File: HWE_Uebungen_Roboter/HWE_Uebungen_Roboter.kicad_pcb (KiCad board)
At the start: 2 copper layers, 3 parts, among them IC1 TB67H450AFNG, U1 ATmega328-P

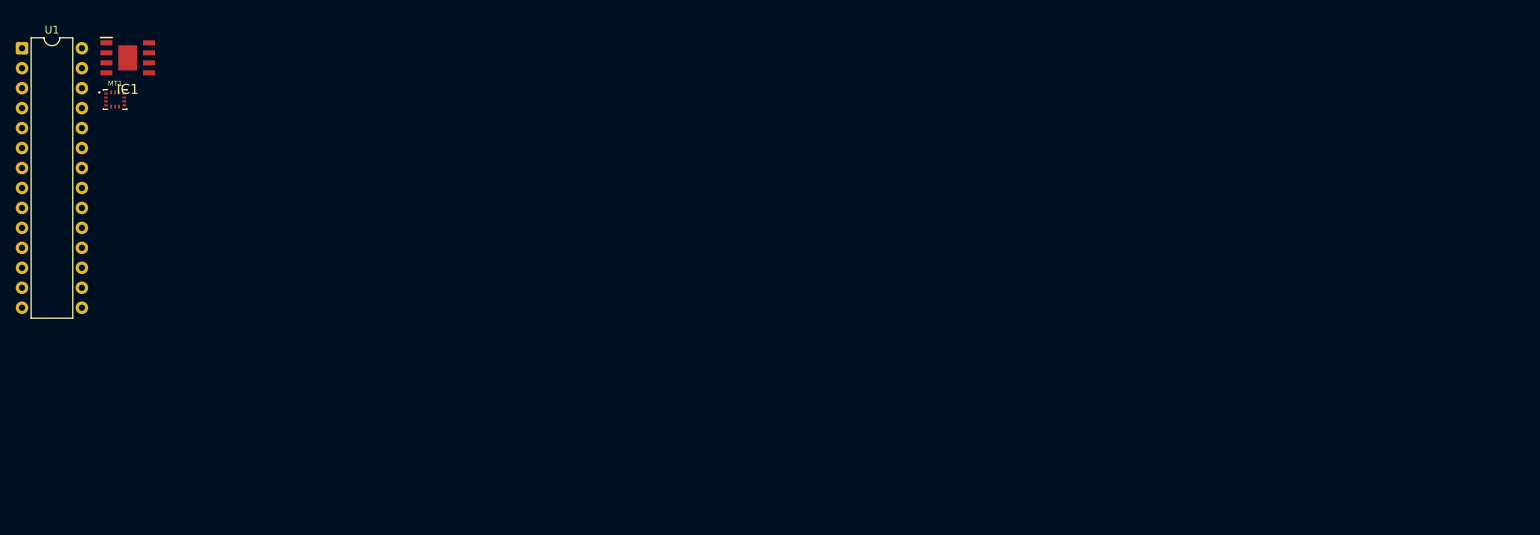
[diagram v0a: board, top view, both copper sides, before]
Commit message: Hardware-Zwischenstand mit KiCad-Projekt und Bestückungsunterlagen
Aktuellen Hardware-Entwicklungsstand des HWE-Roboters von Felix Mähr
und Linus Kimpfler mit bestehender Projektstruktur übernehmen.

Enthalten sind:
- KiCad-Projekt mit Schaltplan und PCB-Layout
- Eigene Symbol- und Footprint-Bibliotheken mit Bibliothekstabellen
- Datenblätter der vorgesehenen Bauteile
- Schaltplan- und PCB-Abbildungen sowie 3D-Vorschau
- Interaktive HTML-Stückliste als Bestückungshilfe

Stand vor der geplanten PCB-Bestellung; das Gesamtprojekt ist noch
nicht abgeschlossen. Softwareentwicklung, Inbetriebnahme und
Funktionsnachweise sind nicht Bestandteil dieses Zwischenstands.

Die ausführliche Projektdokumentation und die .gitignore werden
in einem separaten Commit ergänzt.
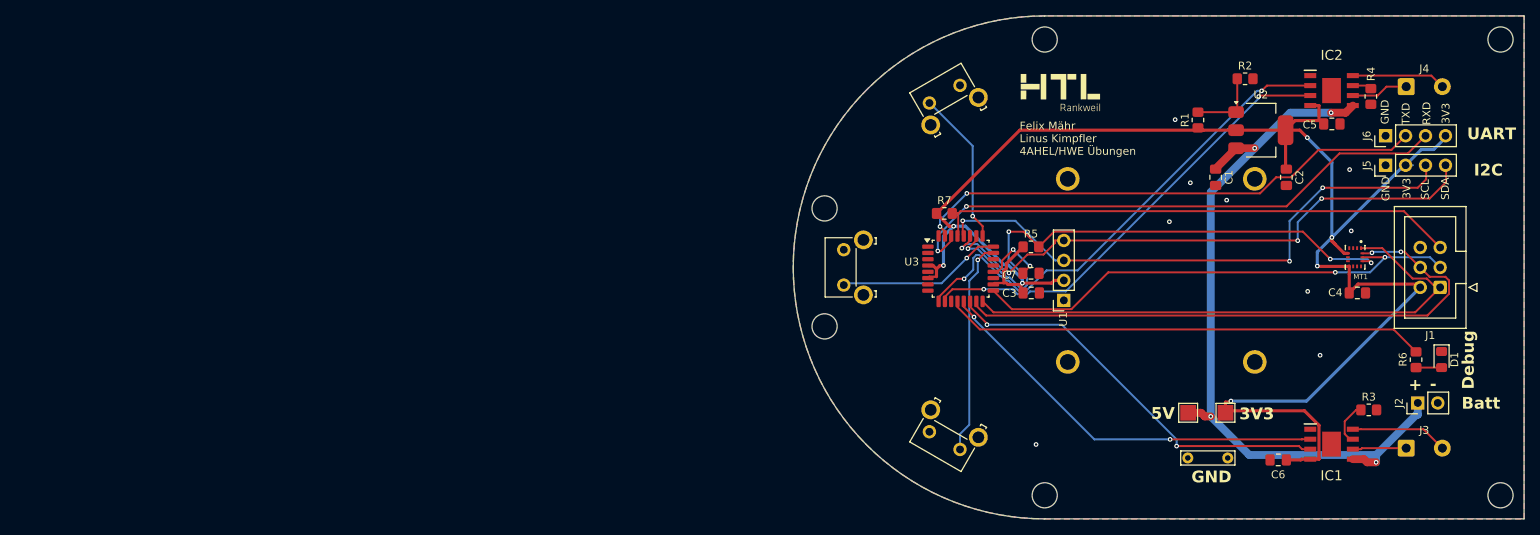
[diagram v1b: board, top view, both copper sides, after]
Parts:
- added C1: C, Capacitor_SMD:C_0805_2012Metric_Pad1.18x1.45mm_HandSolder, F.Cu at (190.5, 64.4)
- added C2: C, Capacitor_SMD:C_0805_2012Metric_Pad1.18x1.45mm_HandSolder, F.Cu at (199.5, 64.4)
- added C3: 100n, Capacitor_SMD:C_0805_2012Metric_Pad1.18x1.45mm_HandSolder, F.Cu at (167.1, 79.1)
- added C4: 100n, Capacitor_SMD:C_0805_2012Metric_Pad1.18x1.45mm_HandSolder, F.Cu at (208.6, 79.1)
- added C5: 100n, Capacitor_SMD:C_0805_2012Metric_Pad1.18x1.45mm_HandSolder, F.Cu at (205.3, 57.6)
- added C6: 100n, Capacitor_SMD:C_0805_2012Metric_Pad1.18x1.45mm_HandSolder, F.Cu at (198.5, 100.4)
- added C7: 100n, Capacitor_SMD:C_0805_2012Metric_Pad1.18x1.45mm_HandSolder, F.Cu at (167.0, 76.6)
- added D1: LED, LED_SMD:LED_0805_2012Metric_Pad1.15x1.40mm_HandSolder, F.Cu at (219.3, 87.6)
- added G***: LOGO, HWE_Lib:HTL_Logo, F.Cu at (170.8, 53.6)
- added H1: MountingHole, MountingHole:MountingHole_3.2mm_M3, F.Cu at (168.8, 46.9)
- added H2: MountingHole, MountingHole:MountingHole_3.2mm_M3, F.Cu at (168.8, 104.9)
- added H3: MountingHole, MountingHole:MountingHole_3.2mm_M3, F.Cu at (140.8, 68.4)
- added H4: MountingHole, MountingHole:MountingHole_3.2mm_M3, F.Cu at (140.8, 83.4)
- added H5: MountingHole, MountingHole:MountingHole_3.2mm_M3, F.Cu at (226.8, 46.9)
- added H6: MountingHole, MountingHole:MountingHole_3.2mm_M3, F.Cu at (226.8, 104.9)
- added IC2: TB67H450AFNG, Robo:P-HSOP8-0405-1.27-002, F.Cu at (205.3, 53.4)
- added J1: AVR-ISP-6, Connector_IDC:IDC-Header_2x03_P2.54mm_Vertical, F.Cu at (222.8, 75.9)
- added J2: Conn_01x02_Pin, Connector_PinHeader_2.54mm:PinHeader_1x02_P2.54mm_Vertical, F.Cu at (216.2, 93.1)
- added J3: Conn_01x02_Pin, Connector_Wire:SolderWire-0.5sqmm_1x02_P4.6mm_D0.9mm_OD2.1mm, F.Cu at (214.8, 98.9)
- added J4: Conn_01x02_Pin, Connector_Wire:SolderWire-0.5sqmm_1x02_P4.6mm_D0.9mm_OD2.1mm, F.Cu at (214.8, 52.9)
- added J5: Conn_01x04_Pin, Connector_PinHeader_2.54mm:PinHeader_1x04_P2.54mm_Vertical, F.Cu at (212.1, 62.9)
- added J6: Conn_01x04_Pin, Connector_PinHeader_2.54mm:PinHeader_1x04_P2.54mm_Vertical, F.Cu at (212.1, 59.1)
- added R1: R, Resistor_SMD:R_0805_2012Metric_Pad1.20x1.40mm_HandSolder, F.Cu at (188.3, 57.1)
- added R2: R, Resistor_SMD:R_0805_2012Metric_Pad1.20x1.40mm_HandSolder, F.Cu at (194.3, 51.9)
- added R3: R, Resistor_SMD:R_0805_2012Metric_Pad1.20x1.40mm_HandSolder, F.Cu at (210.0, 94.0)
- added R4: R, Resistor_SMD:R_0805_2012Metric_Pad1.20x1.40mm_HandSolder, F.Cu at (210.3, 54.1)
- added R5: 100k, Resistor_SMD:R_0805_2012Metric_Pad1.20x1.40mm_HandSolder, F.Cu at (167.0, 73.2)
- added R6: R, Resistor_SMD:R_0805_2012Metric_Pad1.20x1.40mm_HandSolder, F.Cu at (216.0, 87.6)
- added R7: 100k, Resistor_SMD:R_0805_2012Metric_Pad1.20x1.40mm_HandSolder, F.Cu at (156.0, 69.0)
- added SW1: SW_Omron_B3FS, Button_Switch_THT:SW_SPST_Omron_B3F-315x_Angled, F.Cu at (156.8, 96.7)
- added SW2: SW_Omron_B3FS, Button_Switch_THT:SW_SPST_Omron_B3F-315x_Angled, F.Cu at (144.8, 75.9)
- added SW3: SW_Omron_B3FS, Button_Switch_THT:SW_SPST_Omron_B3F-315x_Angled, F.Cu at (156.8, 55.1)
- added TP1: GND, TestPoint:TestPoint_Bridge_Pitch5.08mm_Drill0.7mm, F.Cu at (187.0, 100.1)
- added TP2: 3V3, TestPoint:TestPoint_Pad_2.0x2.0mm, F.Cu at (191.8, 94.4)
- added TP3: 5V, TestPoint:TestPoint_Pad_2.0x2.0mm, F.Cu at (187.0, 94.4)
- added U2: LM317_SOT-223, Package_TO_SOT_SMD:SOT-223-3_TabPin2, F.Cu at (196.3, 58.4)
- added U3: ATmega328P-A, Package_QFP:TQFP-32_7x7mm_P0.8mm, F.Cu at (158.1, 76.0)
- MT1: footprint Robo:BMI323 -> Robo:XDCR_ICM-42670-P
- U1: value ATmega328-P -> OLED_I2C; footprint Package_DIP:DIP-28_W7.62mm -> Robo:OLED_SSD1306_I2C_0.96
- moved IC1 160.9 mm to (205.3, 98.4)
- moved MT1 159.1 mm to (208.3, 74.6), turned to -90 degrees
- moved U1 136.4 mm to (171.2, 80.1), turned to 90 degrees
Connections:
- IC1 pad 1: unconnected-(IC1-GND-Pad1) -> GND
- IC1 pad 2: unconnected-(IC1-IN2-Pad2) -> /Richtung 1 links
- IC1 pad 3: unconnected-(IC1-IN1-Pad3) -> /Richtung 2 links
- IC1 pad 4: unconnected-(IC1-VREF-Pad4) -> +3V3
- IC1 pad 5: unconnected-(IC1-VM-Pad5) -> +BATT
- IC1 pad 6: unconnected-(IC1-OUT1-Pad6) -> Net-(IC1-OUT1)
- IC1 pad 7: unconnected-(IC1-RS-Pad7) -> Net-(IC1-RS)
- IC1 pad 8: unconnected-(IC1-OUT2-Pad8) -> Net-(IC1-OUT2)
- IC1 pad 9: unconnected-(IC1-EP-Pad9) -> GND
- MT1 pad 1: unconnected-(MT1-AP_SDO/AP_AD0-Pad1) -> /MISO
- MT1 pad 10: Net-(MT1-RESV-Pad10) -> unconnected-(MT1-RESV-Pad10)_2
- MT1 pad 11: Net-(MT1-RESV-Pad10) -> unconnected-(MT1-RESV-Pad10)
- MT1 pad 12: unconnected-(MT1-AP_CS-Pad12) -> /CS
- MT1 pad 13: unconnected-(MT1-AP_SCL/AP_SCLK-Pad13) -> /SCK
- MT1 pad 14: unconnected-(MT1-AP_SDA/AP_SDIO/AP_SDI-Pad14) -> /MOSI
- MT1 pad 2: Net-(MT1-RESV-Pad10) -> unconnected-(MT1-RESV-Pad10)_3
- MT1 pad 3: Net-(MT1-RESV-Pad10) -> unconnected-(MT1-RESV-Pad10)_1
- MT1 pad 5: unconnected-(MT1-VDDIO-Pad5) -> +3V3
- MT1 pad 6: unconnected-(MT1-GND-Pad6) -> GND
- MT1 pad 7: unconnected-(MT1-FSYNC-Pad7) -> GND
- MT1 pad 8: unconnected-(MT1-VDD-Pad8) -> +3V3
- U1 pad 1: unconnected-(U1-~{RESET}/PC6-Pad1) -> GND
- U1 pad 2: unconnected-(U1-PD0-Pad2) -> +3V3
- U1 pad 3: unconnected-(U1-PD1-Pad3) -> /SCL
- U1 pad 4: unconnected-(U1-PD2-Pad4) -> /SDA
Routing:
- net +3V3: track 0.00 -> 221.8 mm, vias 0 -> 7
- net +BATT: track 0.00 -> 96.4 mm, vias 0 -> 4
- net /MOSI: track 0.00 -> 76.7 mm, vias 0 -> 2
- net /SDA: track 0.00 -> 73.6 mm, vias 0 -> 4
- net /MISO: track 0.00 -> 72.3 mm
- net /RXD: track 0.00 -> 72.2 mm, vias 0 -> 2
- net /SCL: track 0.00 -> 71.9 mm, vias 0 -> 3
- net /CS: track 0.00 -> 70.2 mm, vias 0 -> 4
- net /RST: track 0.00 -> 67.0 mm
- net /TXD: track 0.00 -> 66.0 mm, vias 0 -> 2
- net /SCK: track 0.00 -> 64.1 mm, vias 0 -> 2
- net /Richtung 1 rechts: track 0.00 -> 63.7 mm, vias 0 -> 2
- net /LED: track 0.00 -> 61.4 mm
- net /Richtung 2 rechts: track 0.00 -> 58.3 mm, vias 0 -> 2
- net /Richtung 2 links: track 0.00 -> 52.1 mm, vias 0 -> 2
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- added copper zone on B.Cu, net GND
- added copper zone on F.Cu, net GND
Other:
- board outline added: 93 x 64 mm
- board text added: "+"
- board text added: "-"
- board text added: "3V3"
- board text added: "5V"
- board text added: "Batt"
- board text added: "Debug"
- board text added: "Felix Mähr Linus Kimpfler 4AHEL/HWE Übungen"
- board text added: "GND"
- board text added: "I2C"
- board text added: "RXD"
- board text added: "SCL"
- board text added: "SDA"
- board text added: "TXD"
- board text added: "UART"
